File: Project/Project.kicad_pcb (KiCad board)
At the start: 2 copper layers, 40 x 40 mm, 24 parts, among them J1 Conn_01x05_Male, J2 USB_OTG, U1 CMWX1ZZABZ-078, U2 LM1117ADJ, Y1 8Mhz

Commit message: some placements put
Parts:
- removed Y1: 8Mhz, Crystal:Crystal_HC49-U_Vertical
- added C16: 4.7u, Capacitor_SMD:C_0805_2012Metric_Pad1.15x1.40mm_HandSolder, F.Cu at (235.5, 242.3)
- added C17: 4.7u, Capacitor_SMD:C_0805_2012Metric_Pad1.15x1.40mm_HandSolder, F.Cu at (291.0, 260.2)
- added C18: 4.7u, Capacitor_SMD:C_0805_2012Metric_Pad1.15x1.40mm_HandSolder, F.Cu at (217.7, 257.0)
- added C19: 10u, Capacitor_SMD:C_0805_2012Metric_Pad1.15x1.40mm_HandSolder, F.Cu at (222.6, 251.5)
- added C20: 10u, Capacitor_SMD:C_0805_2012Metric_Pad1.15x1.40mm_HandSolder, F.Cu at (230.7, 245.2)
- added C21: 100n, Capacitor_SMD:C_0805_2012Metric_Pad1.15x1.40mm_HandSolder, F.Cu at (216.2, 260.0)
- added C22: 10u, Capacitor_SMD:C_0805_2012Metric_Pad1.15x1.40mm_HandSolder, F.Cu at (230.7, 242.3)
- added D1: LED, LED_SMD:LED_0805_2012Metric_Pad1.15x1.40mm_HandSolder, F.Cu at (228.0, 239.3)
- added D2: LED, LED_SMD:LED_0805_2012Metric_Pad1.15x1.40mm_HandSolder, F.Cu at (232.8, 239.3)
- added D3: D_Zener, Diode_SMD:D_SMA_Handsoldering, F.Cu at (220.5, 239.5)
- added J3: Conn_01x09_Male, Connector_PinHeader_2.54mm:PinHeader_1x09_P2.54mm_Horizontal, F.Cu at (287.9, 289.7)
- added J4: Conn_01x03_Female, Connector_JST:JST_PH_B3B-PH-K_1x03_P2.00mm_Vertical, F.Cu at (297.6, 263.7)
- added J5: Conn_Coaxial, Connector_Coaxial:U.FL_Molex_MCRF_73412-0110_Vertical, F.Cu at (252.7, 252.7)
- added R5: 470, Resistor_SMD:R_0805_2012Metric_Pad1.15x1.40mm_HandSolder, F.Cu at (236.8, 251.1)
- added R6: 10k, Resistor_SMD:R_0805_2012Metric_Pad1.15x1.40mm_HandSolder, F.Cu at (260.8, 286.3)
- added R7: 10k, Resistor_SMD:R_0805_2012Metric_Pad1.15x1.40mm_HandSolder, F.Cu at (225.7, 263.3)
- added R8: 2k, Resistor_SMD:R_0805_2012Metric_Pad1.15x1.40mm_HandSolder, F.Cu at (236.8, 254.1)
- added R9: 470, Resistor_SMD:R_0805_2012Metric_Pad1.15x1.40mm_HandSolder, F.Cu at (240.2, 240.1)
- added SW1: SW_Push, Button_Switch_SMD:SW_Push_1P1T_NO_6x6mm_H9.5mm, F.Cu at (261.5, 276.1)
- added SW2: SW_Push, Button_Switch_SMD:SW_Push_1P1T_NO_6x6mm_H9.5mm, F.Cu at (292.4, 278.3)
- added SW3: SW_Push, Button_Switch_SMD:SW_Push_1P1T_NO_6x6mm_H9.5mm, F.Cu at (261.7, 265.6)
- added U3: MCP73831-2-OT, Package_TO_SOT_SMD:SOT-23-5, F.Cu at (289.4, 268.6)
- added U4: TMP36xS, Package_SO:SOIC-8_3.9x4.9mm_P1.27mm, F.Cu at (259.9, 252.9)
- C1: value 18p -> 0.1u
- C2: value 18p -> 10u
- J2: footprint Connector_USB:USB_Mini-B_Wuerth_65100516121_Horizontal -> Connector_USB:USB_Micro-B_Wuerth_629105150521
- R3: value 10k -> 330
- R4: value 3.3k -> 560
- U1: footprint RF_Module:CMWX1ZZABZ -> lab1_CMWX1ZZABZ-078:CMWX1ZZABZ_longer_pads
- moved C11 66.3 mm to (221.0, 260.0), turned to 0 degrees
- moved C15 66.1 mm to (213.2, 246.8), turned to 0 degrees
- moved C14 57.8 mm to (231.9, 233.7), turned to 0 degrees
- moved R4 57.4 mm to (230.5, 257.4), turned to 0 degrees
- moved C12 55.5 mm to (230.7, 248.2), turned to 0 degrees
- moved C8 52.1 mm to (227.3, 254.4), turned to 0 degrees
- moved C9 51.1 mm to (296.9, 287.2), turned to 0 degrees
- moved R2 49.5 mm to (216.2, 263.0), turned to 0 degrees
- moved R3 46.0 mm to (240.2, 246.0), turned to 0 degrees
- moved C13 45.5 mm to (225.7, 260.3), turned to 0 degrees
- moved C2 42.5 mm to (232.1, 254.1), turned to 0 degrees
- moved C7 41.5 mm to (221.0, 262.9), turned to 0 degrees
- moved C1 41.3 mm to (227.3, 251.5), turned to 0 degrees
- moved R1 37.6 mm to (283.8, 286.1), turned to 180 degrees
- moved J2 37.3 mm to (294.7, 255.1), turned to 180 degrees
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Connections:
- net Net-(J1-Pad2) renamed /SWCLK
- net Net-(J1-Pad4) renamed /SWDIO
- C1 pad 1: Net-(C1-Pad1) -> /NRST
- C2 pad 1: Net-(C2-Pad1) -> GND
- C2 pad 2: GND -> Net-(C2-Pad2)
- R1 pad 1: /NRST -> /enable
- R1 pad 2: +3V3 -> Net-(R1-Pad2)
- R3 pad 2: GND -> Net-(R3-Pad2)
- R4 pad 2: GND -> Net-(R3-Pad2)
- U1 pad 18: Net-(U1-Pad18) -> /TX
- U1 pad 19: Net-(U1-Pad19) -> /RX
- U1 pad 21: Net-(U1-Pad21) -> Net-(R1-Pad2)
- U1 pad 22: Net-(U1-Pad22) -> /temperature
- U1 pad 23: Net-(U1-Pad23) -> /3DF(3D-FiX_indicator)
- U1 pad 24: Net-(U1-Pad24) -> /1pps(1_pulse_per_second)
- U1 pad 26: Net-(U1-Pad26) -> Net-(C2-Pad2)
- U1 pad 45: Net-(C2-Pad1) -> Net-(U1-Pad45)
- U1 pad 46: Net-(C1-Pad1) -> Net-(U1-Pad46)
- U2 pad 1: GND -> Net-(R3-Pad2)
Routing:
- net +3V3: track 151.6 -> 0.00 mm, vias 4 -> 0
- net Net-(C10-Pad1): track 36.6 -> 0.00 mm, vias 2 -> 0
- net GND: track 22.2 -> 0.00 mm, vias 3 -> 0
- net /NRST: track 18.9 -> 0.00 mm
- net /SWDIO: track 16.6 -> 0.00 mm, vias 2 -> 0
- net /SWCLK: track 15.6 -> 0.00 mm, vias 2 -> 0
- net Net-(R2-Pad1): track 10.8 -> 0.00 mm, vias 2 -> 0
- net Net-(C2-Pad1): track 9.99 -> 0.00 mm
- net Net-(C1-Pad1): track 9.25 -> 0.00 mm
- removed copper zone on B.Cu, net GND
- removed copper zone on F.Cu, net GND
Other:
- board outline removed

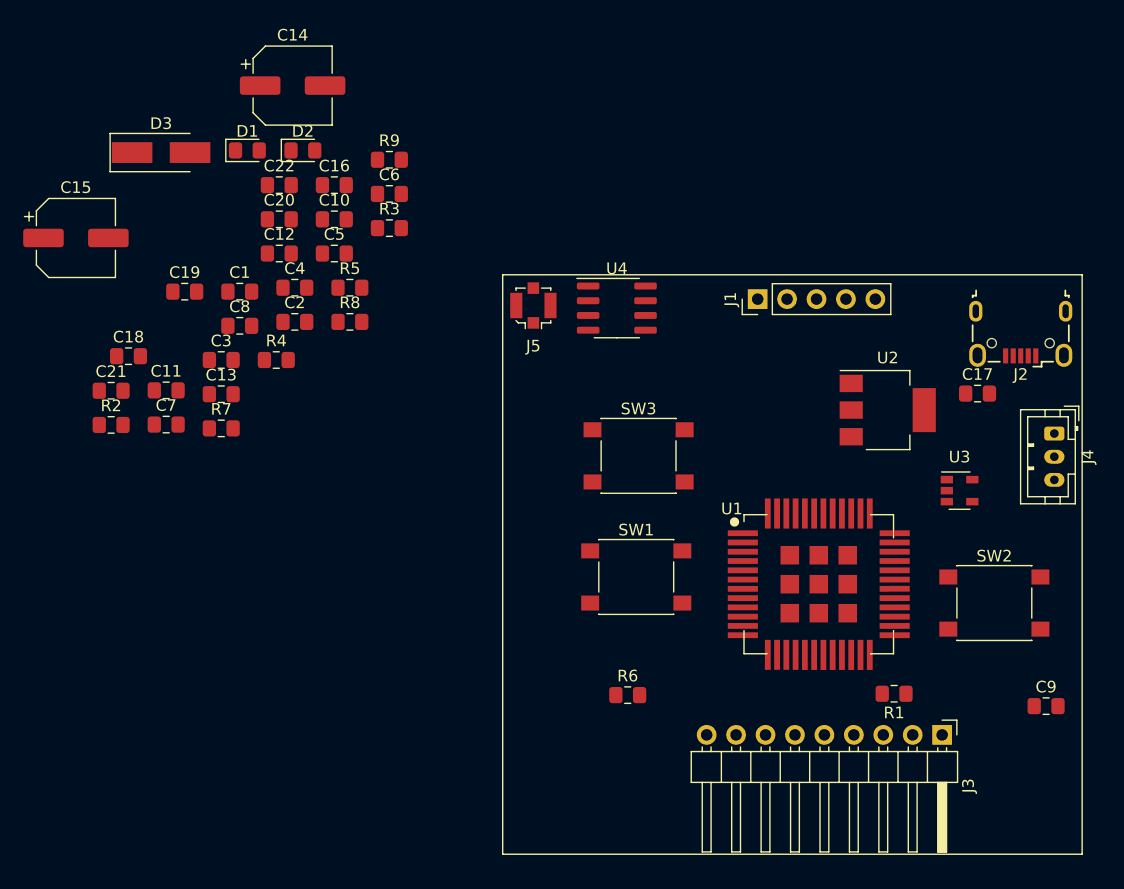
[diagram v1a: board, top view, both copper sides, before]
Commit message: placed all components
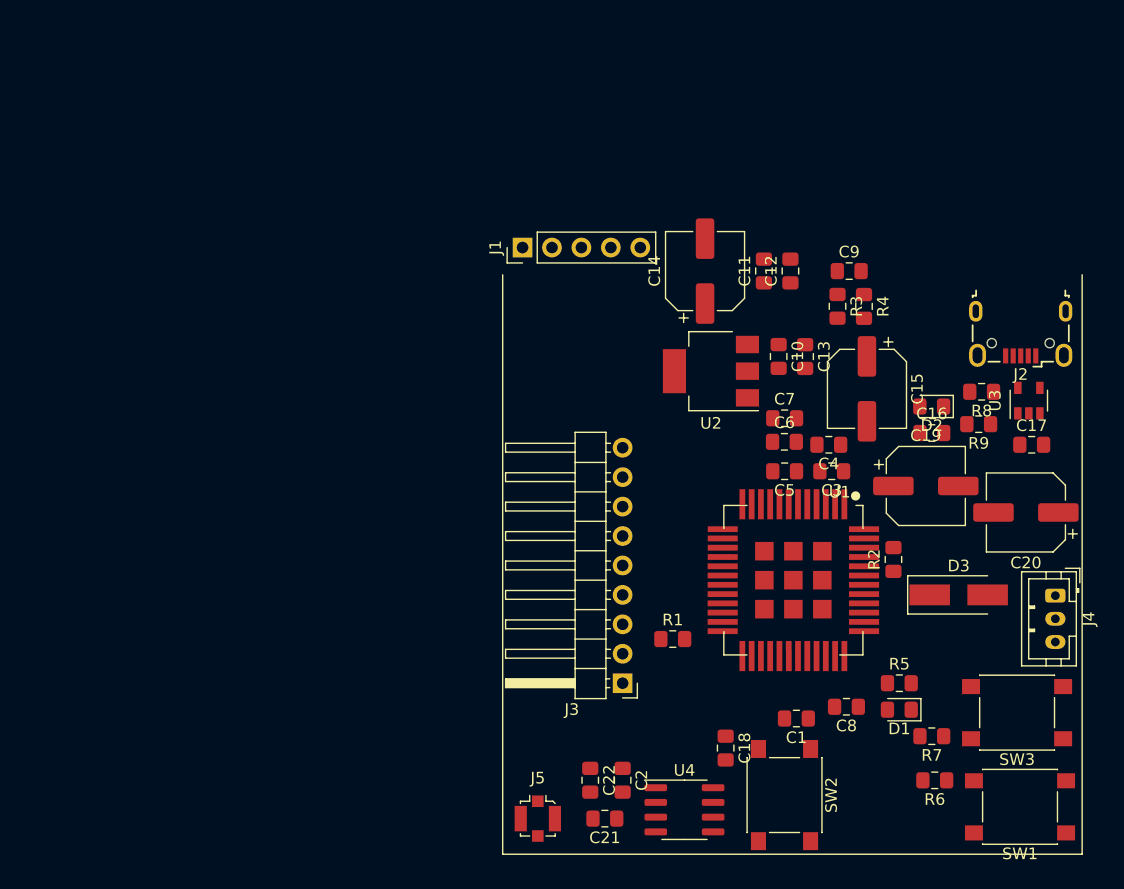
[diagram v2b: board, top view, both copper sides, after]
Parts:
- C19, C20: footprint Capacitor_SMD:C_0805_2012Metric_Pad1.15x1.40mm_HandSolder -> Capacitor_SMD:CP_Elec_6.3x4.9
- moved D3 78.7 mm to (289.3, 277.6)
- moved D1 74.1 mm to (284.2, 287.5), turned to 180 degrees
- moved C15 69.5 mm to (281.4, 259.8), turned to 270 degrees
- moved C20 69.2 mm to (295.1, 270.5), turned to 180 degrees
- moved R2 68.5 mm to (283.7, 274.6), turned to 90 degrees
- moved R7 66.8 mm to (287.0, 289.8), turned to 180 degrees
- moved C19 66.1 mm to (286.5, 268.2)
- moved C8 61.8 mm to (279.7, 287.3), turned to 180 degrees
- moved C18 61.6 mm to (269.2, 290.8), turned to 270 degrees
- moved C1 60.5 mm to (275.3, 288.3), turned to 180 degrees
- moved D2 58.6 mm to (287.0, 261.4), turned to 180 degrees
- moved R5 58.4 mm to (284.2, 285.2)
- moved C22 57.9 mm to (257.6, 293.6), turned to 270 degrees
- moved C21 56.4 mm to (258.8, 296.9), turned to 180 degrees
- moved C16 55.8 mm to (287.0, 263.7)
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
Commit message: started routing
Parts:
- moved J1 55.6 mm to (276.2, 297.6)
- moved U2 17.2 mm to (256.3, 245.7)
- moved U4 14.2 mm to (255.8, 286.0)
- moved J3 10.2 mm to (261.2, 275.1)
- moved J2 9.92 mm to (294.4, 245.2)
- moved R8 7.88 mm to (292.2, 252.3)
- moved U3 7.88 mm to (296.3, 253.0)
- moved C16 7.88 mm to (287.9, 255.8)
- moved C17 7.88 mm to (296.5, 256.8)
- moved D2 7.88 mm to (287.9, 253.5)
- moved R9 7.88 mm to (291.9, 255.1)
- moved C9 7.62 mm to (282.7, 242.6)
- moved R3 7.62 mm to (281.7, 245.7)
- moved R4 7.62 mm to (284.0, 245.7)
- moved C18 7.56 mm to (263.3, 286.2)
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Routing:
- net +3V3: track 0.00 -> 146.3 mm, vias 0 -> 2
- net Net-(C10-Pad1): track 0.00 -> 67.6 mm
- net Net-(C17-Pad2): track 0.00 -> 29.8 mm
- net Net-(R3-Pad2): track 0.00 -> 28.0 mm, vias 0 -> 2
- net /SWCLK: track 0.00 -> 24.4 mm, vias 0 -> 2
- net /SWDIO: track 0.00 -> 21.8 mm, vias 0 -> 2
- net Net-(R7-Pad1): track 0.00 -> 17.4 mm
- net Net-(R5-Pad2): track 0.00 -> 5.80 mm
- net Net-(R9-Pad1): track 0.00 -> 2.74 mm
- net Net-(D2-Pad1): track 0.00 -> 2.64 mm
- net Net-(D1-Pad2): track 0.00 -> 2.29 mm
- net Net-(R8-Pad1): track 0.00 -> 2.24 mm

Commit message: some more routing
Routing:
- net +3V3: track 146.3 -> 174.3 mm, vias 2 -> 4
- net /NRST: track 0.00 -> 22.5 mm, vias 0 -> 1
- net Net-(R6-Pad1): track 0.00 -> 20.5 mm, vias 0 -> 2
- net Net-(C2-Pad2): track 0.00 -> 19.4 mm
- net Net-(C21-Pad2): track 0.00 -> 7.57 mm
- net /enable: track 0.00 -> 0.70 mm
- net /3DF(3D-FiX_indicator): track 0.00 -> 0.60 mm
- net Net-(R1-Pad2): track 0.00 -> 0.53 mm
- net /1pps(1_pulse_per_second): track 0.00 -> 0.52 mm, vias 0 -> 1
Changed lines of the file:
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@@
     (thickness 1.6)
     (drawings 6)
-    (tracks 140)
+    (tracks 194)
     (zones 0)
     (modules 46)
@@
   (segment (start 276.22 296.25) (end 278.638 293.832) (width 0.5) (layer F.Cu) (net 1))
   (segment (start 278.638 287.974) (end 278.638 287.274) (width 0.5) (layer F.Cu) (net 1))
-  (segment (start 276.22 297.6) (end 276.22 296.25) (width 0.5) (layer F.Cu) (net 1))
   (segment (start 276.282 282.902) (end 276.282 282.002) (width 0.5) (layer F.Cu) (net 1))
   (segment (start 276.282 285.493) (end 276.282 282.902) (width 0.5) (layer F.Cu) (net 1))
@@
   (segment (start 275.26 262.288) (end 275.354 262.382) (width 0.5) (layer F.Cu) (net 1))
   (segment (start 275.26 260.34) (end 275.26 262.288) (width 0.5) (layer F.Cu) (net 1))
-  (segment (start 262.500001 273.799999) (end 261.2 275.1) (width 0.5) (layer F.Cu) (net 1))
-  (segment (start 272.804002 260.34) (end 262.500001 270.644001) (width 0.5) (layer F.Cu) (net 1))
-  (segment (start 275.26 260.34) (end 272.804002 260.34) (width 0.5) (layer F.Cu) (net 1))
-  (segment (start 262.500001 270.644001) (end 262.500001 271.870001) (width 0.5) (layer F.Cu) (net 1))
-  (segment (start 262.500001 271.870001) (end 262.500001 273.799999) (width 0.5) (layer F.Cu) (net 1))
   (segment (start 263.155 287.905) (end 259.26 287.905) (width 0.5) (layer F.Cu) (net 1))
   (segment (start 259.26 287.905) (end 258.285 287.905) (width 0.5) (layer F.Cu) (net 1))
@@
   (segment (start 263.98 287.205) (end 263.28 287.205) (width 0.5) (layer F.Cu) (net 1))
   (segment (start 261.2 280.744966) (end 264.43001 283.974976) (width 0.5) (layer F.Cu) (net 1))
+  (segment (start 290.286 290.032) (end 290.411 290.032) (width 0.5) (layer F.Cu) (net 1))
+  (segment (start 289.136 291.182) (end 290.286 290.032) (width 0.5) (layer F.Cu) (net 1))
+  (segment (start 281.288 291.182) (end 289.136 291.182) (width 0.5) (layer F.Cu) (net 1))
+  (segment (start 276.22 296.25) (end 281.288 291.182) (width 0.5) (layer F.Cu) (net 1))
+  (segment (start 276.22 297.6) (end 276.22 296.25) (width 0.5) (layer F.Cu) (net 1))
+  (segment (start 298.615 296.961) (end 298.615 297.01) (width 0.5) (layer F.Cu) (net 1))
+  (segment (start 298.615 297.01) (end 298.615 298.16) (width 0.5) (layer F.Cu) (net 1))
+  (via (at 290.322 291.846) (size 0.8) (drill 0.3) (layers F.Cu B.Cu) (net 1))
+  (segment (start 290.411 290.032) (end 290.411 291.757) (width 0.5) (layer F.Cu) (net 1))
+  (segment (start 290.411 291.757) (end 290.322 291.846) (width 0.5) (layer F.Cu) (net 1))
+  (segment (start 290.322 291.846) (end 290.721999 292.245999) (width 0.5) (layer B.Cu) (net 1))
+  (via (at 289.052 298.196) (size 0.8) (drill 0.3) (layers F.Cu B.Cu) (net 1))
+  (segment (start 290.721999 292.245999) (end 290.721999 296.526001) (width 0.5) (layer B.Cu) (net 1))
+  (segment (start 290.721999 296.526001) (end 289.052 298.196) (width 0.5) (layer B.Cu) (net 1))
+  (segment (start 290.629 298.196) (end 290.665 298.16) (width 0.5) (layer F.Cu) (net 1))
+  (segment (start 289.052 298.196) (end 290.629 298.196) (width 0.5) (layer F.Cu) (net 1))
+  (segment (start 262.55 275.1) (end 261.2 275.1) (width 0.5) (layer B.Cu) (net 1))
+  (segment (start 275.26 262.39) (end 262.55 275.1) (width 0.5) (layer B.Cu) (net 1))
+  (segment (start 275.26 260.34) (end 275.26 262.39) (width 0.5) (layer B.Cu) (net 1))
   (segment (start 276.852 255.312) (end 276.078 255.312) (width 0.5) (layer F.Cu) (net 2))
   (segment (start 281.412 259.872) (end 276.852 255.312) (width 0.5) (layer F.Cu) (net 2))
@@
   (segment (start 297.212 251.928) (end 297.212 250.898) (width 0.5) (layer F.Cu) (net 2))
   (segment (start 297.212 250.898) (end 295.695001 249.381001) (width 0.5) (layer F.Cu) (net 2))
+  (segment (start 276.37 288.99) (end 276.37 288.29) (width 0.2) (layer F.Cu) (net 3))
+  (segment (start 274.72499 289.29001) (end 276.06999 289.29001) (width 0.2) (layer F.Cu) (net 3))
+  (segment (start 273.21 290.805) (end 274.72499 289.29001) (width 0.2) (layer F.Cu) (net 3))
+  (segment (start 276.06999 289.29001) (end 276.37 288.99) (width 0.2) (layer F.Cu) (net 3))
+  (segment (start 272.36 290.805) (end 273.21 290.805) (width 0.2) (layer F.Cu) (net 3))
+  (via (at 277.622 288.29) (size 0.8) (drill 0.3) (layers F.Cu B.Cu) (net 3))
+  (segment (start 276.37 288.29) (end 277.622 288.29) (width 0.2) (layer F.Cu) (net 3))
+  (segment (start 285.530001 296.750001) (end 286.38 297.6) (width 0.2) (layer B.Cu) (net 3))
+  (segment (start 285.229999 296.449999) (end 285.530001 296.750001) (width 0.2) (layer B.Cu) (net 3))
+  (segment (start 280.293997 296.449999) (end 285.229999 296.449999) (width 0.2) (layer B.Cu) (net 3))
+  (segment (start 277.622 293.778002) (end 280.293997 296.449999) (width 0.2) (layer B.Cu) (net 3))
+  (segment (start 277.622 288.29) (end 277.622 293.778002) (width 0.2) (layer B.Cu) (net 3))
+  (segment (start 259.842 295.148) (end 260.35 294.64) (width 0.2) (layer F.Cu) (net 31))
+  (segment (start 259.842 296.926) (end 259.842 295.148) (width 0.2) (layer F.Cu) (net 31))
+  (segment (start 271.482 283.602) (end 271.482 282.902) (width 0.2) (layer F.Cu) (net 31))
+  (segment (start 271.482 284.402) (end 271.482 283.602) (width 0.2) (layer F.Cu) (net 31))
+  (segment (start 261.244 294.64) (end 271.482 284.402) (width 0.2) (layer F.Cu) (net 31))
+  (segment (start 260.35 294.64) (end 261.244 294.64) (width 0.2) (layer F.Cu) (net 31))
+  (segment (start 257.556 295.215) (end 257.556 294.64) (width 0.2) (layer F.Cu) (net 32))
+  (segment (start 257.345 295.426) (end 257.556 295.215) (width 0.2) (layer F.Cu) (net 32))
+  (segment (start 253.033 295.426) (end 257.345 295.426) (width 0.2) (layer F.Cu) (net 32))
+  (segment (start 257.556 296.69) (end 257.792 296.926) (width 0.2) (layer F.Cu) (net 32))
+  (segment (start 257.556 294.64) (end 257.556 296.69) (width 0.2) (layer F.Cu) (net 32))
   (segment (start 283.201 285.942) (end 283.201 287.528) (width 0.2) (layer F.Cu) (net 33))
   (segment (start 283.201 285.242) (end 283.201 285.942) (width 0.2) (layer F.Cu) (net 33))
@@
   (segment (start 278.76 295.64) (end 278.76 297.6) (width 0.2) (layer F.Cu) (net 36))
   (segment (start 279.64 294.76) (end 278.76 295.64) (width 0.2) (layer F.Cu) (net 36))
+  (segment (start 263.652 280.732) (end 263.652 281.432) (width 0.2) (layer F.Cu) (net 37))
+  (segment (start 268.082 279.952) (end 267.482 279.952) (width 0.2) (layer F.Cu) (net 39))
+  (segment (start 268.082 275.952) (end 267.691998 275.952) (width 0.2) (layer F.Cu) (net 40))
+  (segment (start 267.974 276.86) (end 268.082 276.752) (width 0.2) (layer F.Cu) (net 41))
+  (via (at 267.716 282.448) (size 0.8) (drill 0.3) (layers F.Cu B.Cu) (net 42))
+  (segment (start 267.716 281.118) (end 268.082 280.752) (width 0.2) (layer F.Cu) (net 42))
+  (segment (start 265.702 281.432) (end 265.702 280.906) (width 0.2) (layer F.Cu) (net 44))
   (segment (start 283.999 246.676) (end 284.008 246.685) (width 0.2) (layer F.Cu) (net 45))
   (segment (start 281.722 246.676) (end 283.999 246.676) (width 0.2) (layer F.Cu) (net 45))
@@
   (segment (start 282.082 282.073) (end 285.251 285.242) (width 0.2) (layer F.Cu) (net 46))
   (segment (start 282.082 280.752) (end 282.082 282.073) (width 0.2) (layer F.Cu) (net 46))
+  (segment (start 288.344 293.66) (end 288.308 293.624) (width 0.2) (layer F.Cu) (net 47))
+  (segment (start 290.665 293.66) (end 288.344 293.66) (width 0.2) (layer F.Cu) (net 47))
+  (via (at 287.782 292.1) (size 0.8) (drill 0.3) (layers F.Cu B.Cu) (net 47))
+  (segment (start 288.308 293.624) (end 288.308 292.626) (width 0.2) (layer F.Cu) (net 47))
+  (segment (start 288.308 292.626) (end 287.782 292.1) (width 0.2) (layer F.Cu) (net 47))
+  (via (at 286.214525 281.475475) (size 0.8) (drill 0.3) (layers F.Cu B.Cu) (net 47))
+  (segment (start 287.782 292.1) (end 286.214525 290.532525) (width 0.2) (layer B.Cu) (net 47))
+  (segment (start 286.214525 290.532525) (end 286.214525 281.475475) (width 0.2) (layer B.Cu) (net 47))
+  (segment (start 282.472002 279.152) (end 282.082 279.152) (width 0.2) (layer F.Cu) (net 47))
+  (segment (start 284.795477 281.475475) (end 282.472002 279.152) (width 0.2) (layer F.Cu) (net 47))
+  (segment (start 286.214525 281.475475) (end 284.795477 281.475475) (width 0.2) (layer F.Cu) (net 47))
   (segment (start 288.629 289.814) (end 288.054 289.814) (width 0.2) (layer F.Cu) (net 48))
   (segment (start 290.411 288.032) (end 288.629 289.814) (width 0.2) (layer F.Cu) (net 48))

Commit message: all routes done and copperlayer
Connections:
- U1 pad 18: /TX -> /1pps(1_pulse_per_second)
- U1 pad 21: Net-(R1-Pad2) -> /temperature
- U1 pad 22: /temperature -> /TX
- U1 pad 24: /1pps(1_pulse_per_second) -> Net-(R1-Pad2)
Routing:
- net /1pps(1_pulse_per_second): track 0.52 -> 25.7 mm, vias 1 -> 0
- net /RX: track 0.15 -> 18.1 mm
- net /TX: track 0.39 -> 18.3 mm
- net /temperature: track 0.00 -> 17.8 mm, vias 0 -> 2
- net /3DF(3D-FiX_indicator): track 0.60 -> 16.6 mm
- net /enable: track 0.70 -> 11.0 mm
- net +3V3: track 174.3 -> 181.7 mm
- net GND: track 0.00 -> 3.99 mm, vias 0 -> 1
- net Net-(R1-Pad2): track 0.53 -> 3.97 mm
- added copper zone on B.Cu, net GND
- added copper zone on F.Cu, net GND
